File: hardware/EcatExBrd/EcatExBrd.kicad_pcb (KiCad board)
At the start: 6 copper layers, 50 x 50 mm, 173 parts, among them J1 Conn_01x03, J10 Conn_01x06, J11 Conn_01x06, J2 ADM6_ADF6, J3 ADM6_ADF6, J4 Molex_480749101, J5 Molex_480749101, J6 Conn_01x04, J7 Conn_01x06, J8 Conn_01x06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

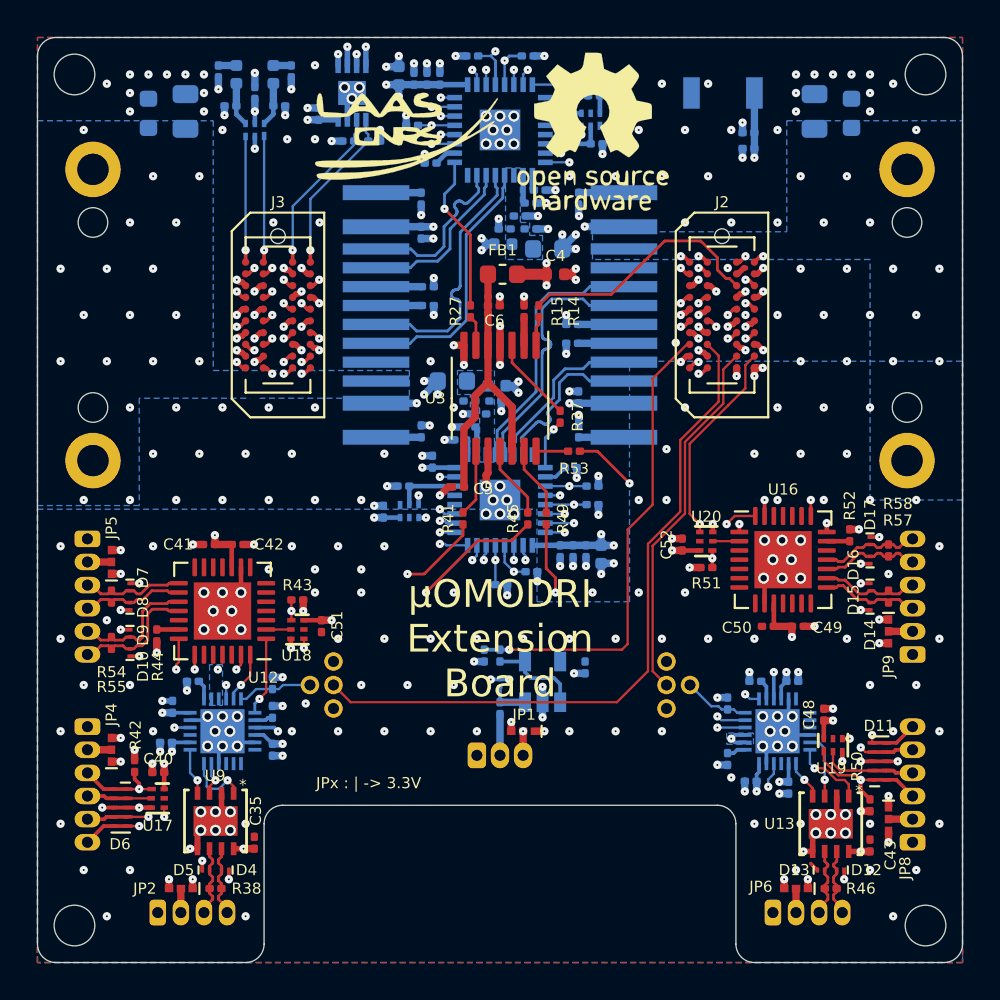
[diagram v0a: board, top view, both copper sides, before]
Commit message: Release 1.1 - Update components values + BOM - Update of J1 pins affectation now matching J2 distribution. - Update gerber files with missing inner layers - Few updates of the PCB layout (J2 redraw + decoupling cap)
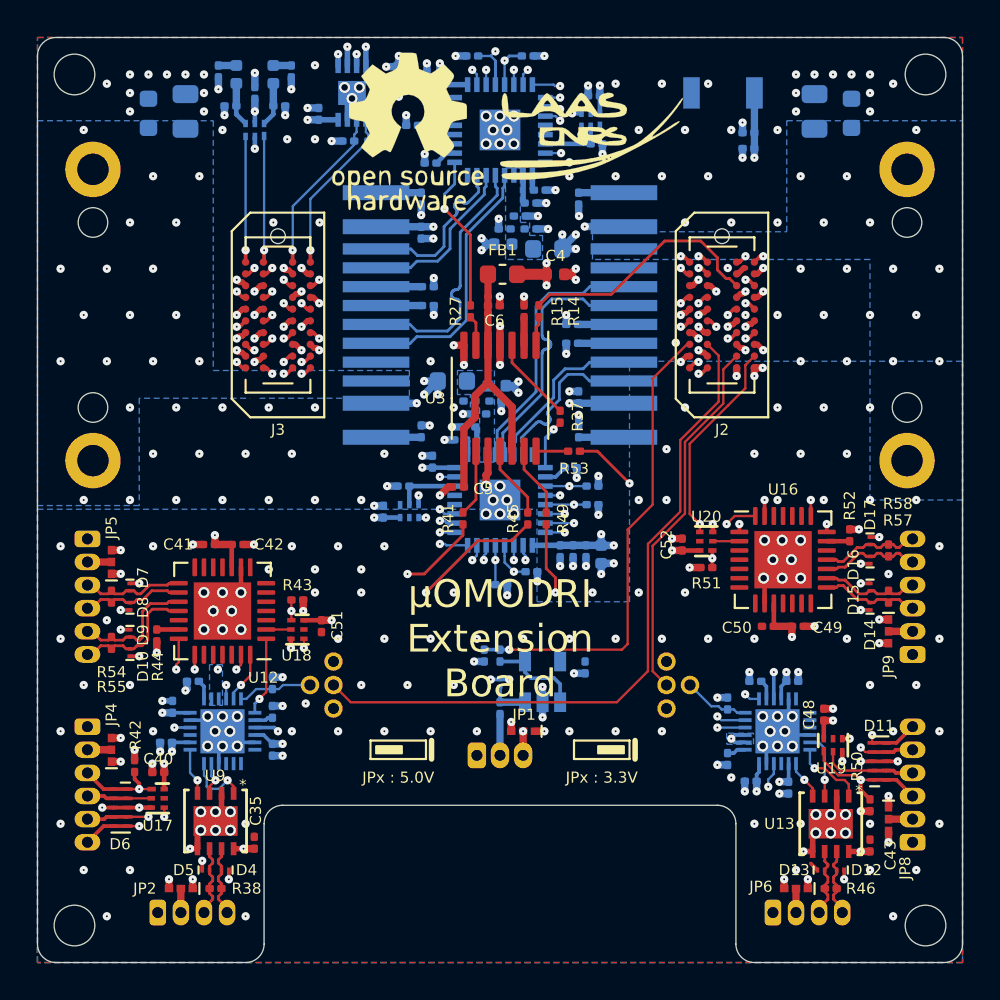
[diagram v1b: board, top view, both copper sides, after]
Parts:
- moved G1 10.0 mm to (130.0, 55.0)
- moved G2 10.0 mm to (120.0, 55.0)
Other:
- board text added: "JPx : 3.3V"
- board text added: "JPx : 5.0V"
- board text removed: "JPx : | -> 3.3V"
